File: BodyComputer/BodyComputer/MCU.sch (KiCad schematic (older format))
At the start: 27 parts

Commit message: Update due to moving to another computer. Updated Schematic, Print-outs, PCB in development
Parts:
- added D36, D37, D38, D39, D40, D41, D42, D43: LED, Diode_SMD:D_0603_1608Metric_Pad1.05x0.95mm_HandSolder, symbol Device:LED
- added R103, R104, R105, R106, R107, R108, R109, R110: 300, Resistor_SMD:R_0603_1608Metric, symbol Device:R
- gave numbers to parts that had none: 27
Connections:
- net GND: now also D36.1 (K), D37.1 (K), D38.1 (K), D39.1 (K), D40.1 (K), D41.1 (K), D42.1 (K), D43.1 (K)
- net Diag_LED_8: now reaches U7.41 (PE10)
- net Diag_LED_8: now also R103.1
- net Diag_LED_7: now reaches U7.43 (PE12)
- net Diag_LED_7: now also R104.1
- net Diag_LED_6: now reaches U7.46 (PE15)
- net Diag_LED_6: now also R105.1
- net Diag_LED_5: now reaches U7.81 (PD0)
- net Diag_LED_5: now also R106.1
- net Diag_LED_4: now reaches U7.82 (PD1)
- net Diag_LED_4: now also R107.1
- net Diag_LED_3: now reaches U7.84 (PD3)
- net Diag_LED_3: now also R108.1
- net Diag_LED_2: now reaches U7.85 (PD4)
- net Diag_LED_2: now also R109.1
- net Diag_LED_1: now reaches U7.88 (PD7)
- net Diag_LED_1: now also R110.1
- new net: D43.2 (A), R110.2
- new net: D42.2 (A), R109.2
- new net: D41.2 (A), R108.2
- new net: D40.2 (A), R107.2
- new net: D39.2 (A), R106.2
- new net: D38.2 (A), R105.2
- new net: D37.2 (A), R104.2
- new net: D36.2 (A), R103.2
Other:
- note added: "Diagnostic LEDs"

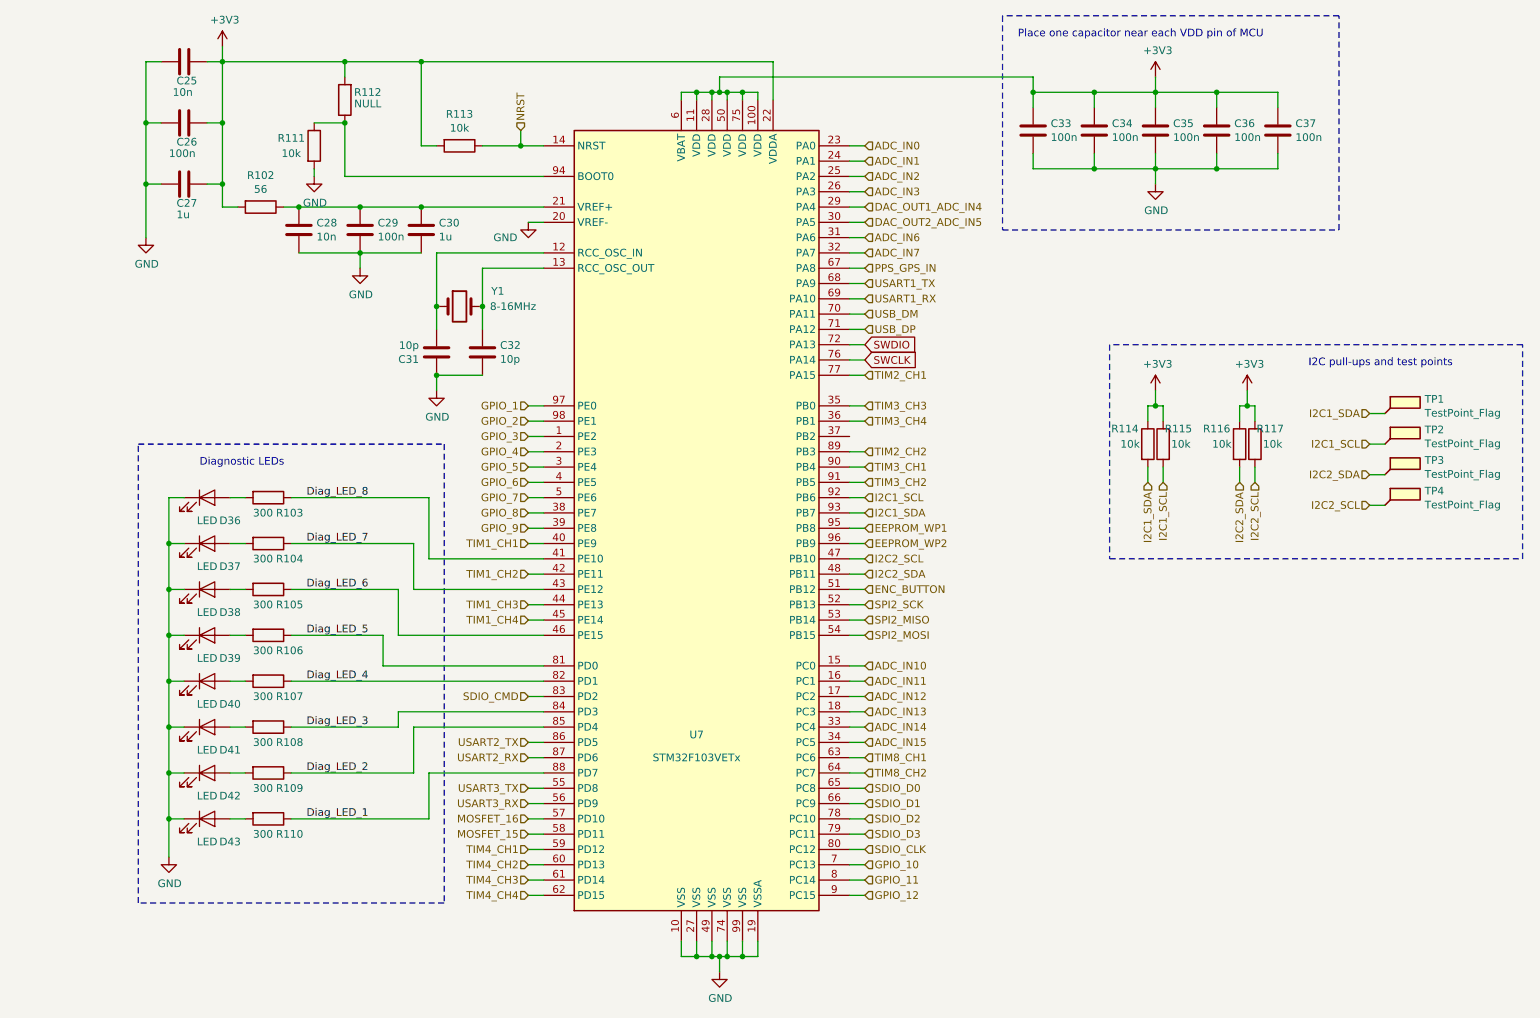
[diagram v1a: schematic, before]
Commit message: Updated schematic (DC/DC), 2-layer PCB
Updated schematic in multiple places, added elements, exchanged 3V3 stabilizer for a DC/DC converter. Nearly finished 2-layer PCB layout.
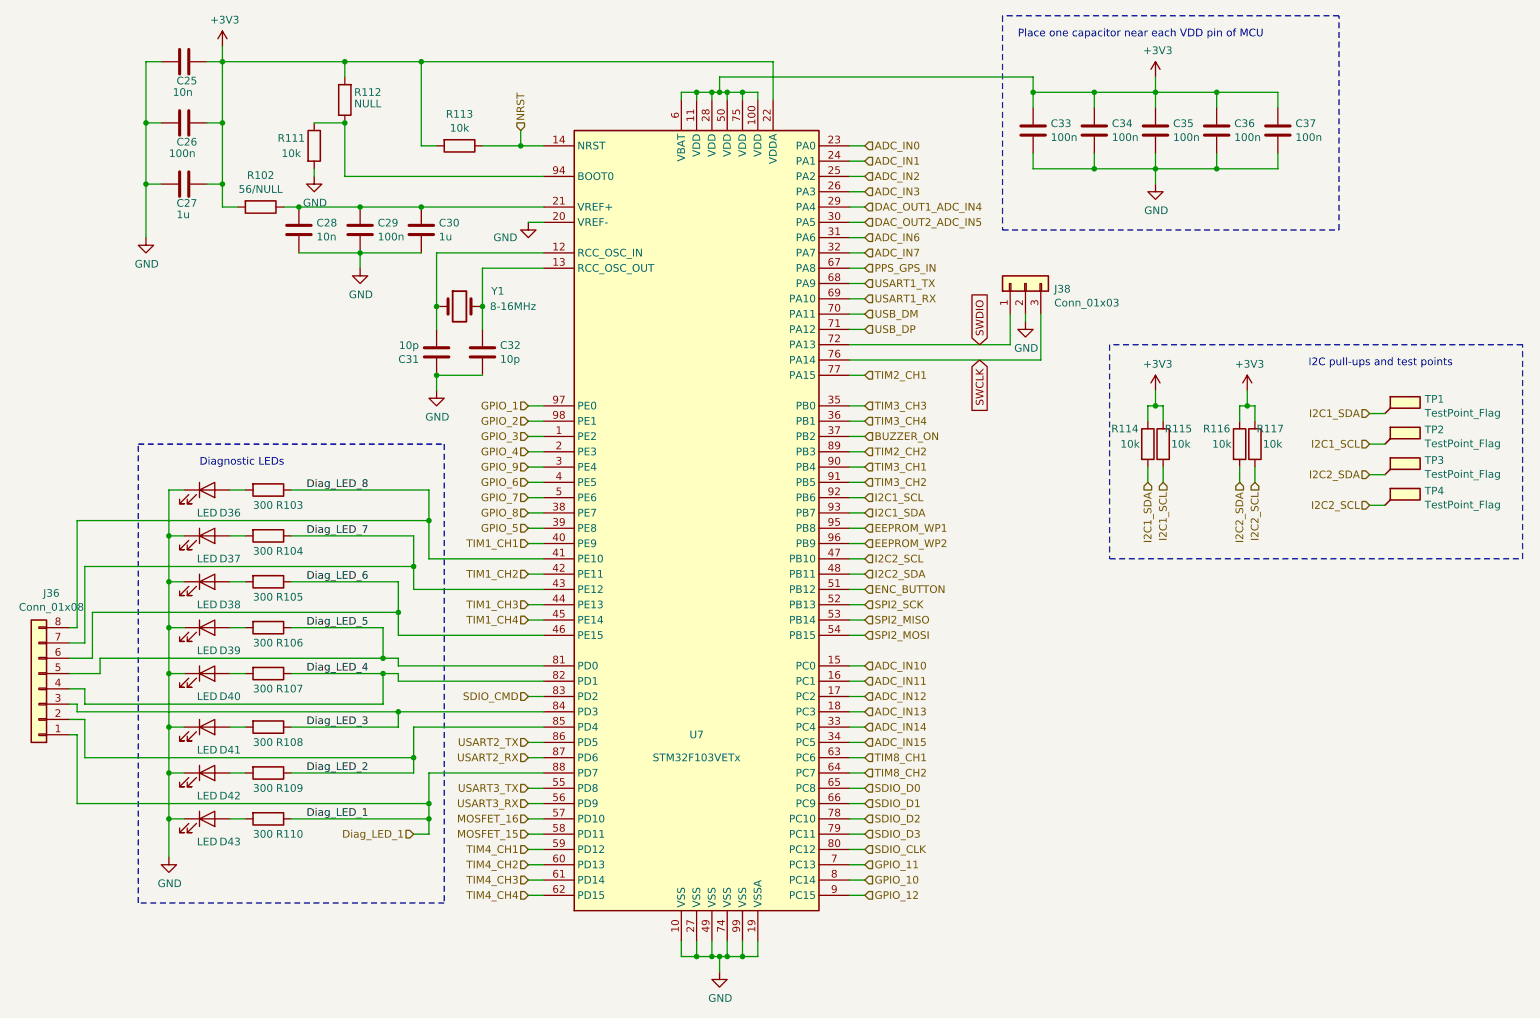
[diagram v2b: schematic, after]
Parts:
- added J36: Conn_01x08, Connector_PinHeader_2.54mm:PinHeader_1x08_P2.54mm_Vertical, symbol Connector_Generic:Conn_01x08
- added J38: Conn_01x03, Connector_PinHeader_2.54mm:PinHeader_1x03_P2.54mm_Vertical, symbol Connector_Generic:Conn_01x03
- R102: value 56 -> 56/NULL
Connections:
- net Diag_LED_1: now also J36.1 (Pin_1)
- net Diag_LED_2: now also J36.2 (Pin_2)
- net Diag_LED_3: now also J36.3 (Pin_3)
- net Diag_LED_4: now also J36.4 (Pin_4)
- net Diag_LED_5: now also J36.5 (Pin_5)
- net Diag_LED_6: now also J36.6 (Pin_6)
- net Diag_LED_7: now also J36.7 (Pin_7)
- net Diag_LED_8: now also J36.8 (Pin_8)
- net GND: now also J38.2 (Pin_2)
- net GPIO_10: now also U7.8 (PC14); no longer U7.7 (PC13)
- net GPIO_11: now also U7.7 (PC13); no longer U7.8 (PC14)
- net GPIO_5: now also U7.39 (PE8); no longer U7.3 (PE4)
- net GPIO_9: now also U7.3 (PE4); no longer U7.39 (PE8)
- net SWCLK: now also J38.3 (Pin_3)
- net SWDIO: now also J38.1 (Pin_1)
- net BUZZER_ON: now reaches U7.37 (PB2)
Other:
- moved on the sheet: D36, D37, D38, D39, D40, R103, R104, R105, R106, R107

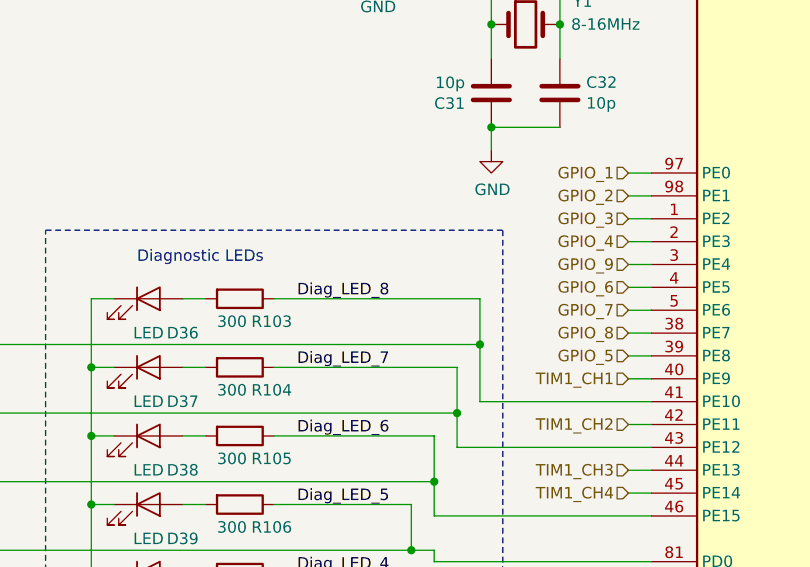
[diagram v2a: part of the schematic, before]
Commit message: Body Computer - 4layer
Added 4-layer board layout, changed schematic a bit, added jumper for NodeMCU powering, control MOSFET for Fans
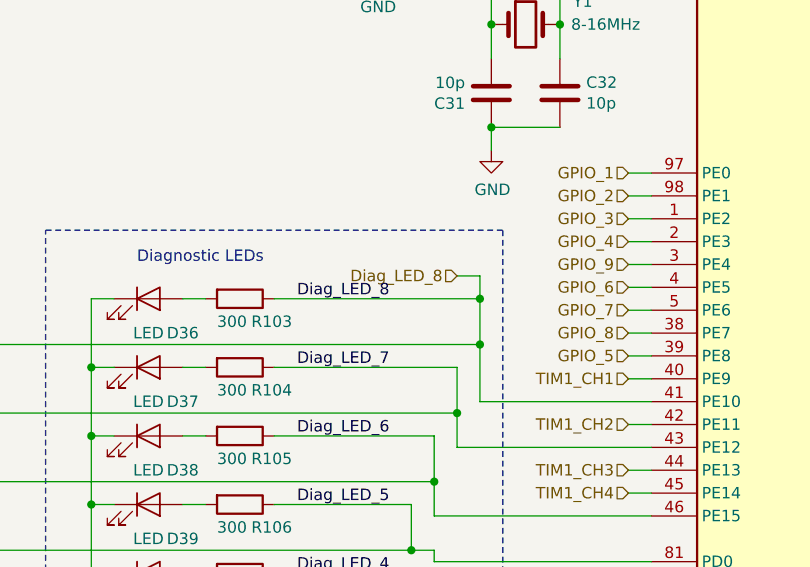
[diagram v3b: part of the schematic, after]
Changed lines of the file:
@@
 Sheet 6 7
 Title "Body Computer"
-Date "2020-04-01"
+Date "2020-04-12"
 Rev "1.0"
 Comp "Wojciech Grzeliński"
@@
 Wire Wire Line
 	7150 2800 7150 2750
+Wire Wire Line
+	3250 3900 3250 3800
+Wire Wire Line
+	3250 3800 3150 3800
+Connection ~ 3250 3900
+Text HLabel 3150 3800 0    50   Input ~ 0
+Diag_LED_8
 $EndSCHEMATC
